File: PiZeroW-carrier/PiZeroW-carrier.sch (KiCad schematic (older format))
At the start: 0 parts

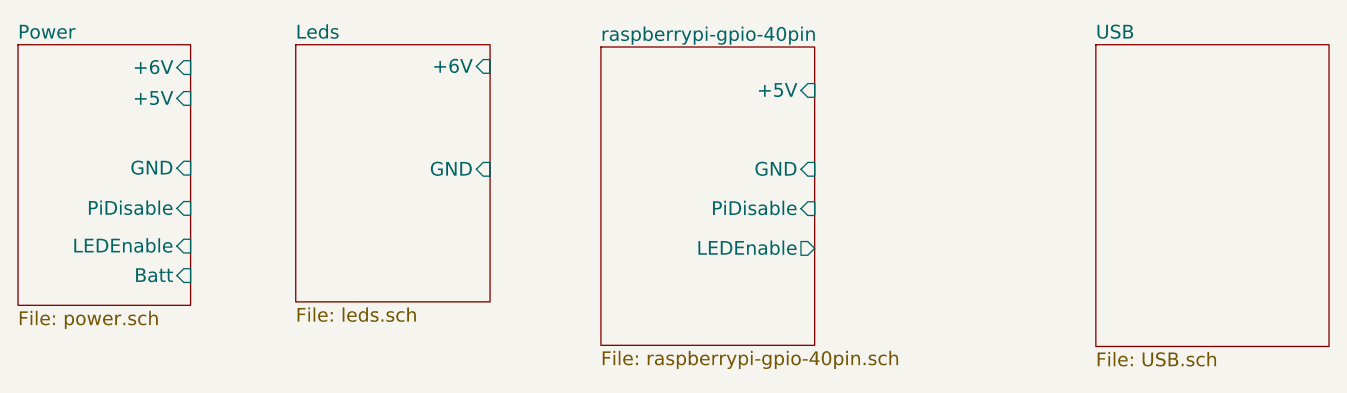
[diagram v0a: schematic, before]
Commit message: cleanup some routes that the autorouter must have created
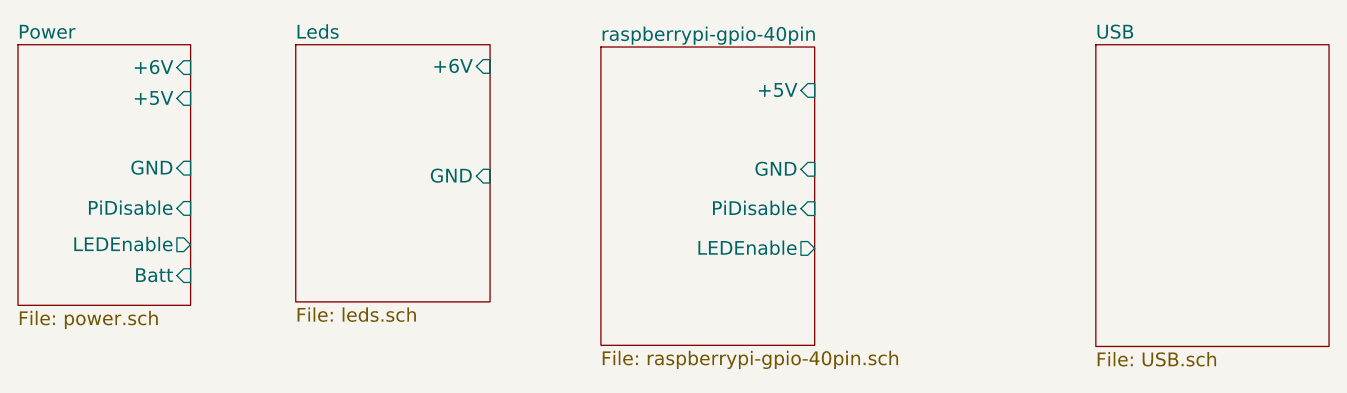
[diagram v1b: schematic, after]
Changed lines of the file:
@@
 F4 "+6V" I R 1900 1300 60
 F5 "+5V" I R 1900 1435 60
-F6 "LEDEnable" I R 1900 2081 60
-F7 "PiDisable" I R 1900 1916 60
+F6 "PiDisable" I R 1900 1916 60
+F7 "LEDEnable" O R 1900 2075 60
 $EndSheet
 $Sheet
@@
 F1 "leds.sch" 60
 F2 "+6V" I R 3210 1295 60
-F3 "GND" I R 3210 1745 60
+F3 "GND" I R 3210 1775 60
 $EndSheet
 $Sheet
